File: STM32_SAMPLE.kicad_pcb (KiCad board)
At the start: 2 copper layers, 49.4 x 34.2 mm, 42 parts, among them J1 USB_B_Micro, J2 Conn_01x03_Male, J3 Conn_01x03_Male, J4 Conn_01x05_Male, J5 Conn_01x02_Male, SW1 SW_Push, U1 LM1117-3.3, U2 STM32F405RGTx

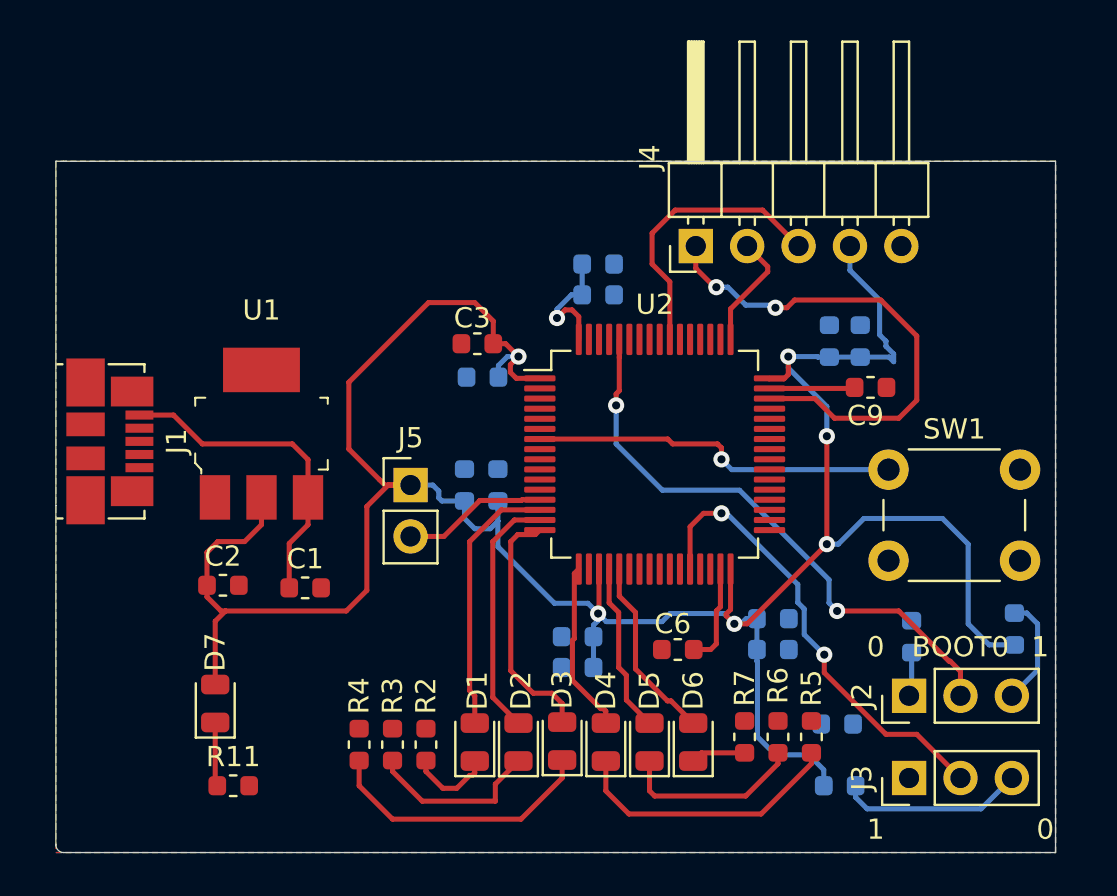
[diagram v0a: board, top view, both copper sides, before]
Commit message: grounding of top and bottom planes
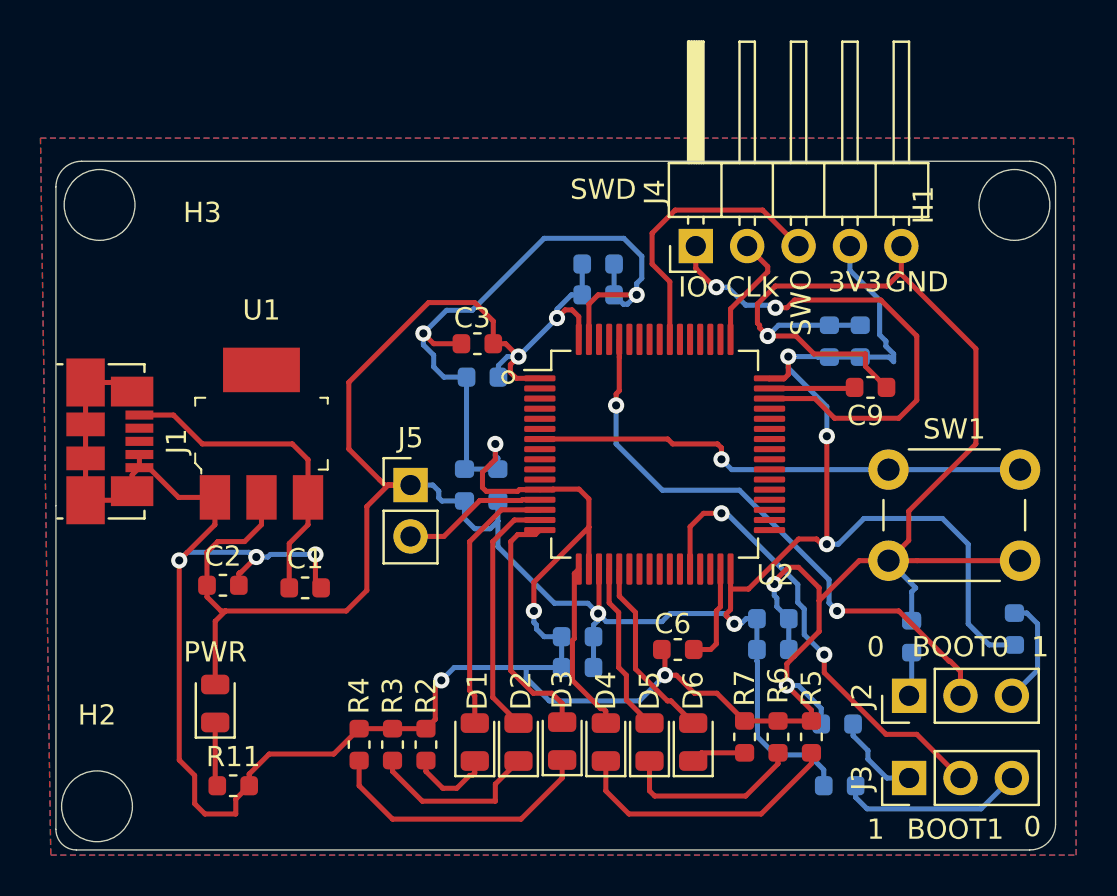
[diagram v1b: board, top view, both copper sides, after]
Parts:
- added H1: MountingHole, MountingHole:MountingHole_3.5mm, F.Cu at (128.9, 106.3)
- added H2: MountingHole, MountingHole:MountingHole_3.5mm, F.Cu at (83.6, 136.0)
- added H3: MountingHole, MountingHole:MountingHole_3.5mm, F.Cu at (83.7, 106.3)
- renumbered D7 to PWR
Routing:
- net GND: track 0.00 -> 213.3 mm, vias 0 -> 12
- net NRST: track 18.2 -> 24.7 mm
- net Net-(J3-Pad1): track 0.00 -> 4.46 mm
- net +3V3: track 141.7 -> 144.0 mm
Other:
- board size 49.4 x 34.2 mm -> 49.4 x 34 mm
- board text added: "3V3"
- board text added: "BOOT1"
- board text added: "CLK"
- board text added: "GND"
- board text added: "IO"
- board text added: "SWD"
- board text added: "SWO"
